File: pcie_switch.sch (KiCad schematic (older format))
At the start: 75 parts, among them J4 Conn_01x03_Male, U2 PI7C9X2G404SL

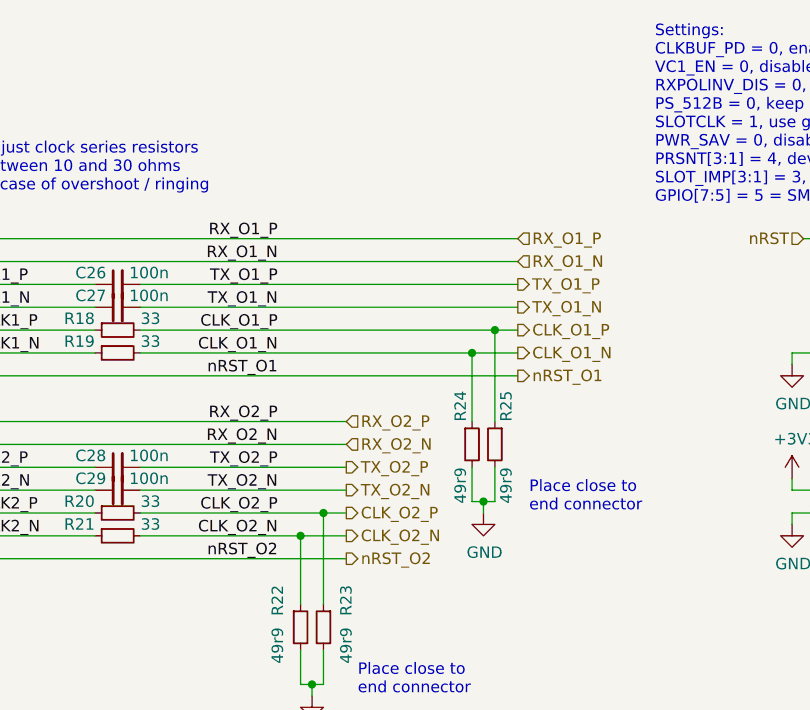
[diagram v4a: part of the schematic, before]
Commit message: sch: Swap some PCIe switch pairs for routing reasons
- Swap clock outputs
- Swap data polarities
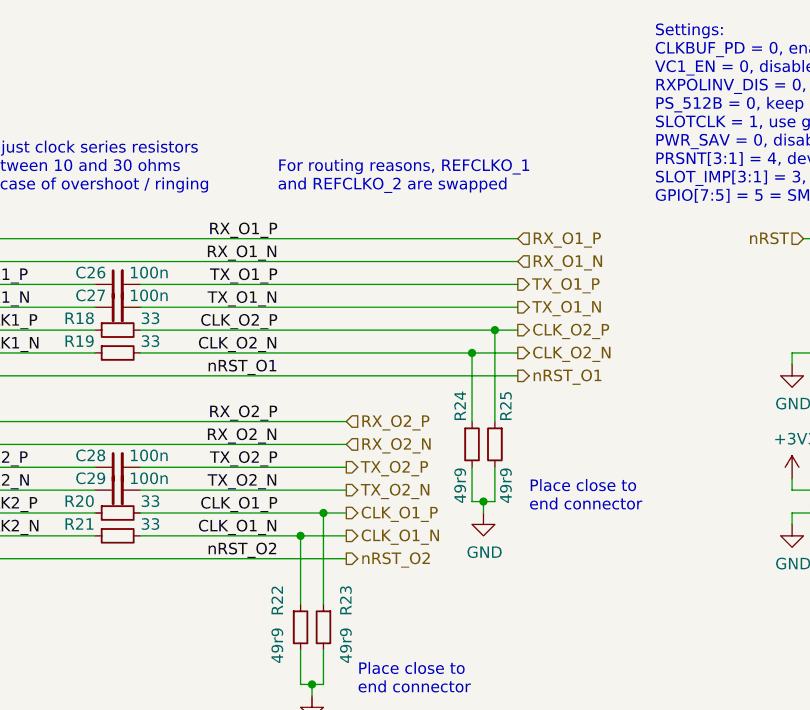
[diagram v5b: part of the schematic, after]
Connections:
- net CLK_O1_N: now also R21.2, R22.1; no longer R19.2, R24.1
- net CLK_O1_P: now also R20.2, R23.1; no longer R18.2, R25.1
- net CLK_O2_N: now also R19.2, R24.1; no longer R21.2, R22.1
- net CLK_O2_P: now also R18.2, R25.1; no longer R20.2, R23.1
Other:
- note added: "For routing reasons, REFCLKO_1\nand REFCLKO_2 are swapped"
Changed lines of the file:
@@
 TX_O1_N
 Text HLabel 6200 1900 2    50   Output ~ 0
-CLK_O1_P
+CLK_O2_P
 Text HLabel 6200 2000 2    50   Output ~ 0
-CLK_O1_N
+CLK_O2_N
 Text Label 5150 1900 2    50   ~ 0
-CLK_O1_P
+CLK_O2_P
 Text Label 5150 2000 2    50   ~ 0
-CLK_O1_N
+CLK_O2_N
 Wire Wire Line
 	6200 2100 3800 2100
@@
 TX_O2_N
 Text HLabel 5450 2700 2    50   Output ~ 0
-CLK_O2_P
+CLK_O1_P
 Text HLabel 5450 2800 2    50   Output ~ 0
-CLK_O2_N
+CLK_O1_N
 Text Label 5150 2700 2    50   ~ 0
-CLK_O2_P
-Text Label 5150 2800 2    50   ~ 0
-CLK_O2_N
+CLK_O1_P
 Wire Wire Line
 	5450 2900 3800 2900
@@
 Wire Wire Line
 	3800 2600 4350 2600
-$Comp
-L Device:R_Small R22
-U 1 1 5D930A7A
-P 5250 3200
-F 0 "R22" V 5150 3250 50  0000 L CNN
-F 1 "49r9" V 5150 3200 50  0000 R CNN
-F 2 "Resistor_SMD:R_0402_1005Metric" H 5250 3200 50  0001 C CNN
-F 3 "~" H 5250 3200 50  0001 C CNN
-	1    5250 3200
-	1    0    0    -1
-$EndComp
-$Comp
-L Device:R_Small R23
-U 1 1 5D9310A8
-P 5350 3200
-F 0 "R23" V 5250 3250 50  0000 L CNN
-F 1 "49r9" V 5250 3200 50  0000 R CNN
-F 2 "Resistor_SMD:R_0402_1005Metric" H 5350 3200 50  0001 C CNN
-F 3 "~" H 5350 3200 50  0001 C CNN
-	1    5350 3200
-	-1   0    0    -1
-$EndComp
 Wire Wire Line
 	5250 3100 5250 2800
@@
 	1    5300 3500
 	1    0    0    -1
-$EndComp
-$Comp
-L Device:R_Small R24
-U 1 1 5D99029B
-P 6000 2400
-F 0 "R24" V 5950 2500 50  0000 L CNN
-F 1 "49r9" V 5950 2300 50  0000 R CNN
-F 2 "Resistor_SMD:R_0402_1005Metric" H 6000 2400 50  0001 C CNN
-F 3 "~" H 6000 2400 50  0001 C CNN
-	1    6000 2400
-	1    0    0    -1
-$EndComp
-$Comp
-L Device:R_Small R25
-U 1 1 5D9902A2
-P 6100 2400
-F 0 "R25" V 6050 2500 50  0000 L CNN
-F 1 "49r9" V 6050 2300 50  0000 R CNN
-F 2 "Resistor_SMD:R_0402_1005Metric" H 6100 2400 50  0001 C CNN
-F 3 "~" H 6100 2400 50  0001 C CNN
-	1    6100 2400
-	-1   0    0    -1
 $EndComp
 Wire Wire Line
@@
 	2700 4700 2700 4800
 Connection ~ 2700 4700
+$Comp
+L Device:R_Small R23
+U 1 1 5D9310A8
+P 5350 3200
+F 0 "R23" V 5250 3250 50  0000 L CNN
+F 1 "49r9" V 5250 3200 50  0000 R CNN
+F 2 "Resistor_SMD:R_0402_1005Metric" H 5350 3200 50  0001 C CNN
+F 3 "~" H 5350 3200 50  0001 C CNN
+	1    5350 3200
+	-1   0    0    -1
+$EndComp
+$Comp
+L Device:R_Small R22
+U 1 1 5D930A7A
+P 5250 3200
+F 0 "R22" V 5150 3250 50  0000 L CNN
+F 1 "49r9" V 5150 3200 50  0000 R CNN
+F 2 "Resistor_SMD:R_0402_1005Metric" H 5250 3200 50  0001 C CNN
+F 3 "~" H 5250 3200 50  0001 C CNN
+	1    5250 3200
+	1    0    0    -1
+$EndComp
+$Comp
+L Device:R_Small R25
+U 1 1 5D9902A2
+P 6100 2400
+F 0 "R25" V 6050 2500 50  0000 L CNN
+F 1 "49r9" V 6050 2300 50  0000 R CNN
+F 2 "Resistor_SMD:R_0402_1005Metric" H 6100 2400 50  0001 C CNN
+F 3 "~" H 6100 2400 50  0001 C CNN
+	1    6100 2400
+	-1   0    0    -1
+$EndComp
+$Comp
+L Device:R_Small R24
+U 1 1 5D99029B
+P 6000 2400
+F 0 "R24" V 5950 2500 50  0000 L CNN
+F 1 "49r9" V 5950 2300 50  0000 R CNN
+F 2 "Resistor_SMD:R_0402_1005Metric" H 6000 2400 50  0001 C CNN
+F 3 "~" H 6000 2400 50  0001 C CNN
+	1    6000 2400
+	1    0    0    -1
+$EndComp
+Text Label 5150 2800 2    50   ~ 0
+CLK_O1_N
+Text Notes 5150 1300 0    50   ~ 0
+For routing reasons, REFCLKO_1\nand REFCLKO_2 are swapped
 $EndSCHEMATC

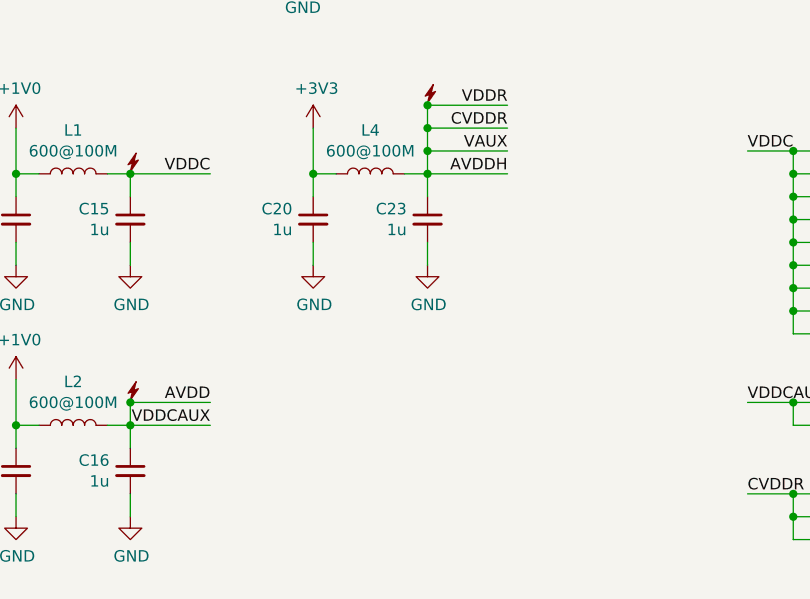
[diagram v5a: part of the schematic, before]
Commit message: sch, pcb: Add testpads on lots of signals
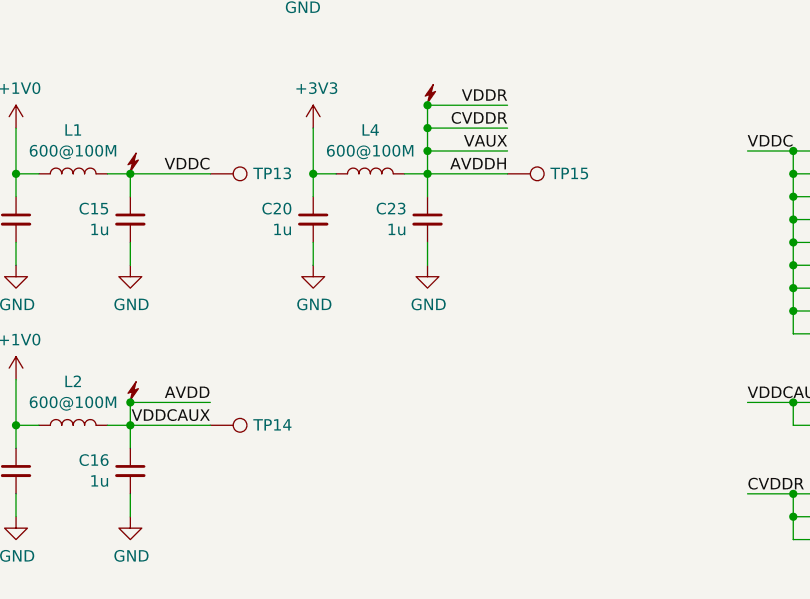
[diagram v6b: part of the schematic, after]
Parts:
- added TP13, TP14, TP15: TestPoint, TestPoint:TestPoint_Pad_D1.0mm, symbol Connector:TestPoint
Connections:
- net AVDD: now also TP14.1
- net AVDDH: now also TP15.1
- net VDDC: now also TP13.1
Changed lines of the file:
@@
 Text Notes 5150 1300 0    50   ~ 0
 For routing reasons, REFCLKO_1\nand REFCLKO_2 are swapped
+$Comp
+L Connector:TestPoint TP?
+U 1 1 5D386A61
+P 1750 5900
+AR Path="/5D05A5E1/5D386A61" Ref="TP?"  Part="1"
+AR Path="/5CE77C37/5D386A61" Ref="TP?"  Part="1"
+AR Path="/5C91A44F/5D5418D5/5D386A61" Ref="TP14"  Part="1"
+F 0 "TP14" V 1750 6088 50  0000 L CNN
+F 1 "TestPoint" V 1795 6088 50  0001 L CNN
+F 2 "TestPoint:TestPoint_Pad_D1.0mm" H 1950 5900 50  0001 C CNN
+F 3 "~" H 1950 5900 50  0001 C CNN
+	1    1750 5900
+	0    1    1    0
+$EndComp
+$Comp
+L Connector:TestPoint TP?
+U 1 1 5D3AA306
+P 1750 4800
+AR Path="/5D05A5E1/5D3AA306" Ref="TP?"  Part="1"
+AR Path="/5CE77C37/5D3AA306" Ref="TP?"  Part="1"
+AR Path="/5C91A44F/5D5418D5/5D3AA306" Ref="TP13"  Part="1"
+F 0 "TP13" V 1750 4988 50  0000 L CNN
+F 1 "TestPoint" V 1795 4988 50  0001 L CNN
+F 2 "TestPoint:TestPoint_Pad_D1.0mm" H 1950 4800 50  0001 C CNN
+F 3 "~" H 1950 4800 50  0001 C CNN
+	1    1750 4800
+	0    1    1    0
+$EndComp
+$Comp
+L Connector:TestPoint TP?
+U 1 1 5D3CD98D
+P 3050 4800
+AR Path="/5D05A5E1/5D3CD98D" Ref="TP?"  Part="1"
+AR Path="/5CE77C37/5D3CD98D" Ref="TP?"  Part="1"
+AR Path="/5C91A44F/5D5418D5/5D3CD98D" Ref="TP15"  Part="1"
+F 0 "TP15" V 3050 4988 50  0000 L CNN
+F 1 "TestPoint" V 3095 4988 50  0001 L CNN
+F 2 "TestPoint:TestPoint_Pad_D1.0mm" H 3250 4800 50  0001 C CNN
+F 3 "~" H 3250 4800 50  0001 C CNN
+	1    3050 4800
+	0    1    1    0
+$EndComp
 $EndSCHEMATC

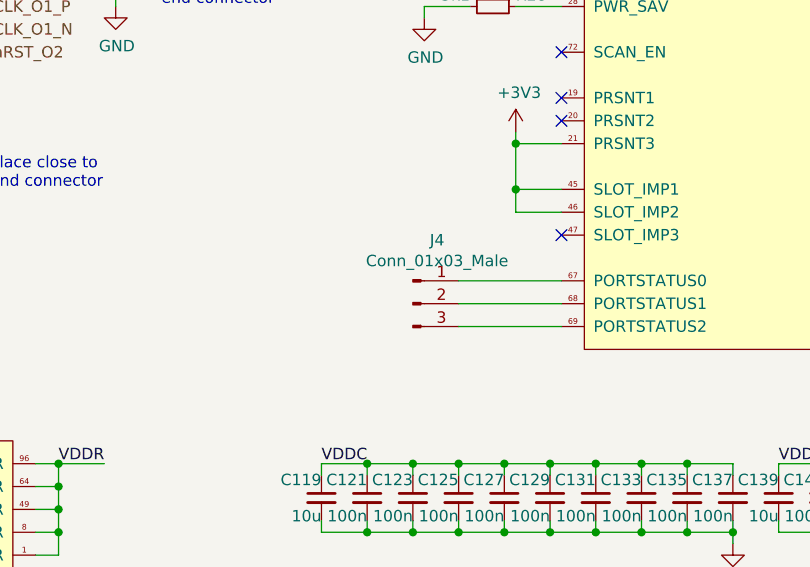
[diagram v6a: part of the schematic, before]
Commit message: sch: Changed PCIe switch debug header to test pads
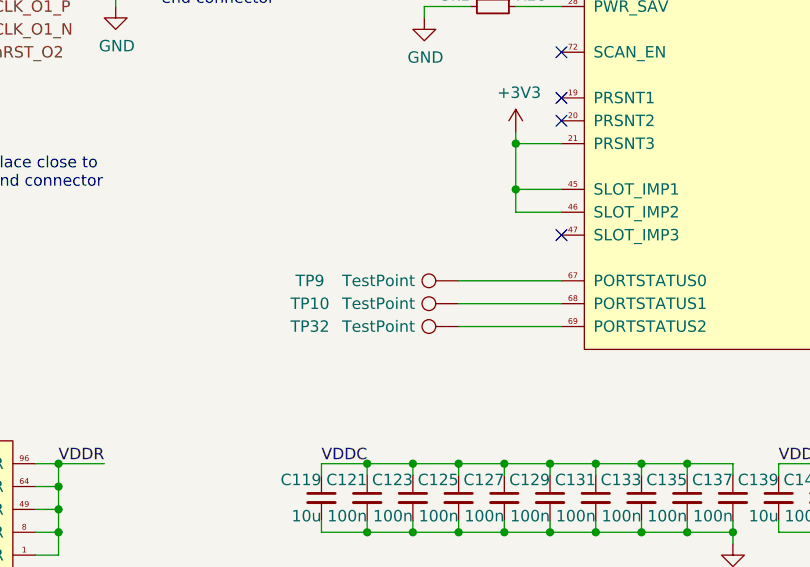
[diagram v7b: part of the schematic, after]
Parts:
- removed J4: Conn_01x03_Male, Connector_PinHeader_2.54mm:PinHeader_1x03_P2.54mm_Vertical, symbol Connector:Conn_01x03_Male
- added TP10, TP32, TP9: TestPoint, TestPoint:TestPoint_Pad_D1.0mm, symbol Connector:TestPoint
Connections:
- net at U2.67 (PORTSTATUS0): now also TP9.1
- net at U2.68 (PORTSTATUS1): now also TP10.1
- net at U2.69 (PORTSTATUS2): now also TP32.1
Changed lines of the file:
@@
 Wire Wire Line
 	7800 3500 7800 3600
-$Comp
-L Connector:Conn_01x03_Male J4
-U 1 1 5D55B632
-P 7350 4000
-F 0 "J4" H 7456 4278 50  0000 C CNN
-F 1 "Conn_01x03_Male" H 7456 4187 50  0000 C CNN
-F 2 "Connector_PinHeader_2.54mm:PinHeader_1x03_P2.54mm_Vertical" H 7350 4000 50  0001 C CNN
-F 3 "~" H 7350 4000 50  0001 C CNN
-	1    7350 4000
-	1    0    0    -1
-$EndComp
 Wire Wire Line
 	7550 3900 8000 3900
@@
 	0    1    1    0
 $EndComp
+$Comp
+L Connector:TestPoint TP9
+U 1 1 5E4195E3
+P 7550 3900
+F 0 "TP9" V 7550 4550 50  0000 C CNN
+F 1 "TestPoint" V 7550 4250 50  0000 C CNN
+F 2 "TestPoint:TestPoint_Pad_D1.0mm" H 7750 3900 50  0001 C CNN
+F 3 "~" H 7750 3900 50  0001 C CNN
+	1    7550 3900
+	0    -1   -1   0
+$EndComp
+$Comp
+L Connector:TestPoint TP10
+U 1 1 5E41B0B3
+P 7550 4000
+F 0 "TP10" V 7550 4650 50  0000 C CNN
+F 1 "TestPoint" V 7550 4350 50  0000 C CNN
+F 2 "TestPoint:TestPoint_Pad_D1.0mm" H 7750 4000 50  0001 C CNN
+F 3 "~" H 7750 4000 50  0001 C CNN
+	1    7550 4000
+	0    -1   -1   0
+$EndComp
+$Comp
+L Connector:TestPoint TP32
+U 1 1 5E41B2C8
+P 7550 4100
+F 0 "TP32" V 7550 4750 50  0000 C CNN
+F 1 "TestPoint" V 7550 4450 50  0000 C CNN
+F 2 "TestPoint:TestPoint_Pad_D1.0mm" H 7750 4100 50  0001 C CNN
+F 3 "~" H 7750 4100 50  0001 C CNN
+	1    7550 4100
+	0    -1   -1   0
+$EndComp
 $EndSCHEMATC

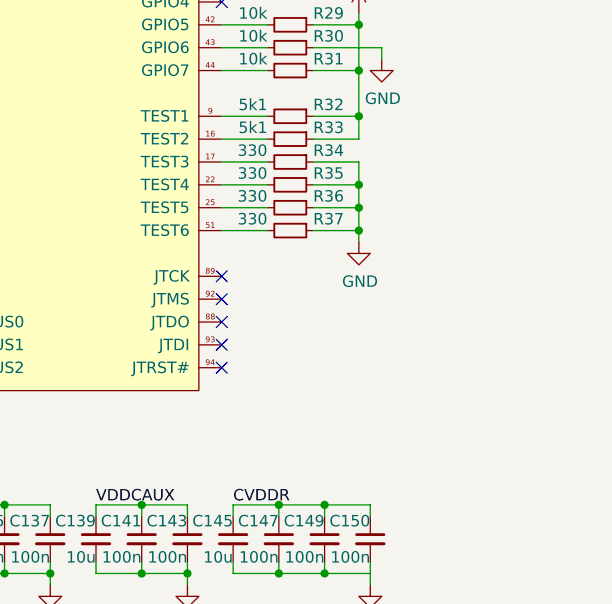
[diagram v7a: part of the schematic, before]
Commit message: sch, pcb: Replace large JTAG headers with 1.27 ones
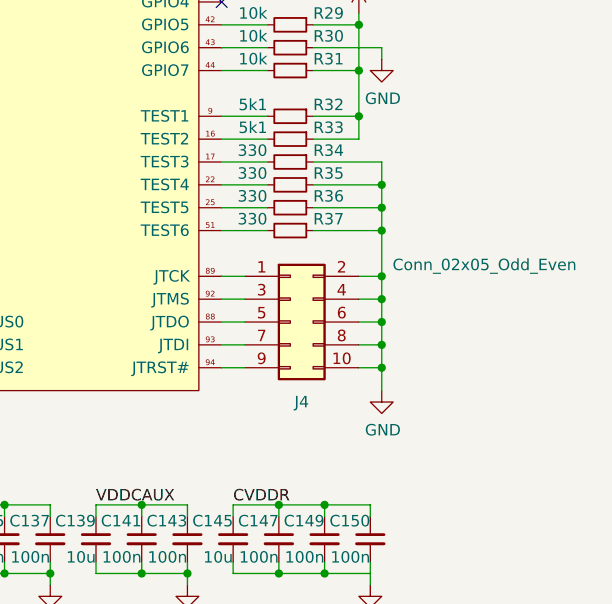
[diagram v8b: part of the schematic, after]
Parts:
- added J4: Conn_02x05_Odd_Even, Connector_PinHeader_1.27mm:PinHeader_2x05_P1.27mm_Vertical_SMD, symbol Connector_Generic:Conn_02x05_Odd_Even
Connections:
- net GND: now also J4.10 (Pin_10), J4.2 (Pin_2), J4.4 (Pin_4), J4.6 (Pin_6), J4.8 (Pin_8)
- net at U2.88 (JTDO): now also J4.5 (Pin_5)
- net at U2.89 (JTCK): now also J4.1 (Pin_1)
- net at U2.92 (JTMS): now also J4.3 (Pin_3)
- net at U2.93 (JTDI): now also J4.7 (Pin_7)
- net at U2.94 (JTRST#): now also J4.9 (Pin_9)
- no-connect marks 27 -> 22
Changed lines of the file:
@@
 Wire Wire Line
 	7550 4100 8000 4100
-NoConn ~ 9500 3700
-NoConn ~ 9500 3800
-NoConn ~ 9500 3900
-NoConn ~ 9500 4000
-NoConn ~ 9500 4100
 $Comp
 L Device:R_Small R32
@@
 L power:GND #PWR062
 U 1 1 5D564AE4
-P 10100 3550
-F 0 "#PWR062" H 10100 3300 50  0001 C CNN
-F 1 "GND" H 10105 3377 50  0000 C CNN
-F 2 "" H 10100 3550 50  0001 C CNN
-F 3 "" H 10100 3550 50  0001 C CNN
-	1    10100 3550
+P 10200 4200
+F 0 "#PWR062" H 10200 3950 50  0001 C CNN
+F 1 "GND" H 10205 4027 50  0000 C CNN
+F 2 "" H 10200 4200 50  0001 C CNN
+F 3 "" H 10200 4200 50  0001 C CNN
+	1    10200 4200
 	1    0    0    -1
 $EndComp
@@
 Connection ~ 10100 3000
 Wire Wire Line
-	9900 3200 10100 3200
-Wire Wire Line
-	10100 3200 10100 3300
-Wire Wire Line
-	9900 3300 10100 3300
-Connection ~ 10100 3300
-Wire Wire Line
-	10100 3300 10100 3400
-Wire Wire Line
-	9900 3400 10100 3400
-Connection ~ 10100 3400
-Wire Wire Line
-	10100 3400 10100 3500
-Wire Wire Line
-	9900 3500 10100 3500
-Connection ~ 10100 3500
-Wire Wire Line
-	10100 3500 10100 3550
+	9900 3200 10200 3200
+Wire Wire Line
+	10200 3200 10200 3300
+Wire Wire Line
+	9900 3300 10200 3300
+Connection ~ 10200 3300
+Wire Wire Line
+	10200 3300 10200 3400
+Wire Wire Line
+	9900 3400 10200 3400
+Connection ~ 10200 3400
+Wire Wire Line
+	10200 3400 10200 3500
+Wire Wire Line
+	9900 3500 10200 3500
 NoConn ~ 9500 2100
 NoConn ~ 9500 2200
@@
 	0    -1   -1   0
 $EndComp
+Wire Wire Line
+	9500 3700 9600 3700
+Wire Wire Line
+	9500 3800 9600 3800
+Wire Wire Line
+	9500 4000 9600 4000
+Wire Wire Line
+	9500 3900 9600 3900
+$Comp
+L Connector_Generic:Conn_02x05_Odd_Even J4
+U 1 1 5DDE825B
+P 9800 3900
+F 0 "J4" H 9850 3550 50  0000 C CNN
+F 1 "Conn_02x05_Odd_Even" H 10650 4150 50  0000 C CNN
+F 2 "Connector_PinHeader_1.27mm:PinHeader_2x05_P1.27mm_Vertical_SMD" H 9800 3900 50  0001 C CNN
+F 3 "~" H 9800 3900 50  0001 C CNN
+	1    9800 3900
+	1    0    0    -1
+$EndComp
+Wire Wire Line
+	9500 4100 9600 4100
+Wire Wire Line
+	10200 4100 10200 4200
+Wire Wire Line
+	10100 4100 10200 4100
+Connection ~ 10200 4100
+Wire Wire Line
+	10200 4000 10200 4100
+Wire Wire Line
+	10200 4000 10100 4000
+Connection ~ 10200 4000
+Wire Wire Line
+	10200 3900 10200 4000
+Wire Wire Line
+	10100 3900 10200 3900
+Connection ~ 10200 3900
+Wire Wire Line
+	10200 3800 10200 3900
+Wire Wire Line
+	10200 3800 10100 3800
+Connection ~ 10200 3800
+Wire Wire Line
+	10200 3700 10200 3800
+Wire Wire Line
+	10100 3700 10200 3700
+Connection ~ 10200 3700
+Connection ~ 10200 3500
+Wire Wire Line
+	10200 3500 10200 3700
 $EndSCHEMATC
